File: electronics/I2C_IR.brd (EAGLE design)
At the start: 11 x 15.9 mm, 10 parts

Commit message: Revised board layout
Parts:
- removed U$1: ADC081C021, mes_adc:MSOP8_0.65
- added U1: ADC081C021, mes_adc:MSOP8_0.65
- moved C2 9.19 mm to (2.20, 3.30), turned to 180 degrees
- moved C4 1.80 mm to (8.70, 9.50), turned to 270 degrees
- moved C1 1.80 mm to (5.60, 3.30)
- moved C3 1.00 mm to (1.40, 9.50)
- moved JP3 1.00 mm to (5.50, 12.9)
- moved R1 1.00 mm to (2.90, 9.50)
- moved SJ1 1.00 mm to (1.50, 6.00)
- moved SJ2 1.00 mm to (9.50, 6.00)
- moved JP1 0.50 mm to (5.50, 1.10)
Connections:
- net ADR0: now also U1.3; no longer U$1.3
- net ADR1: now also U1.6; no longer U$1.6
- net ALERT: now also U1.2; no longer U$1.2
- net GND: now also U1.7; no longer U$1.7
- net N$4: now also U1.4; no longer U$1.4
- net SCL: now also U1.1; no longer U$1.1
- net SDA: now also U1.8; no longer U$1.8
- net VCC: now also U1.5; no longer U$1.5
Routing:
- net VCC: track 21.5 -> 36.2 mm
- net ADR1: track 5.62 -> 6.72 mm
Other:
- board size 11 x 15.9 mm -> 11 x 15.4 mm

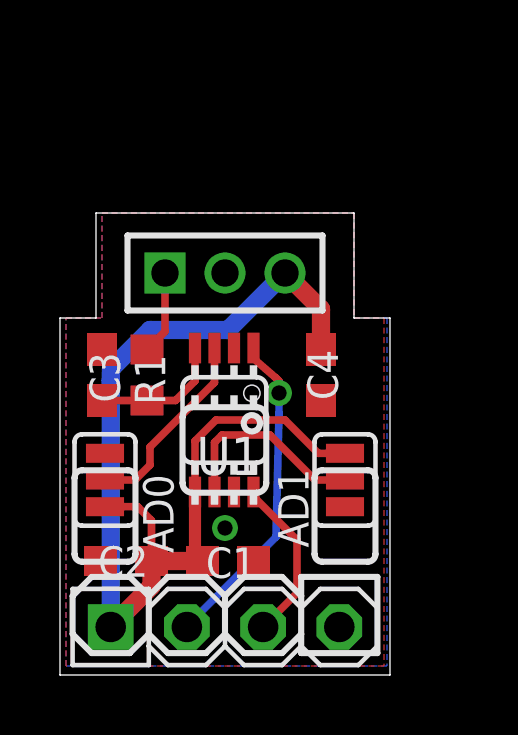
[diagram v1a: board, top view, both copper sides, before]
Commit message: Revised board layout per datasheet, single ground plane with join at chip ground location, no bottom traces, use tantalum bypass caps, etc.
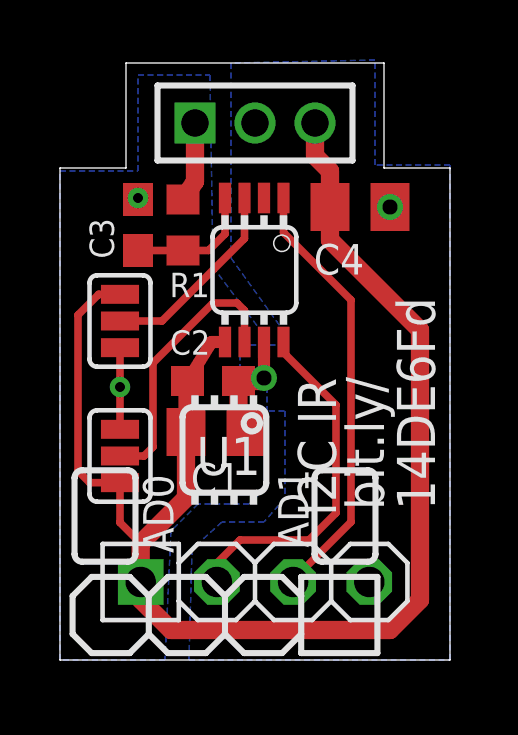
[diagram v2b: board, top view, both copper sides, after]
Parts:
- C1, C4: device rcl:C0603 -> rcl:C0805K
- SJ1: value ADR0 -> AD0
- SJ2: value ADR1 -> AD1
- moved SJ2 7.54 mm to (2.00, 6.80), turned to 90 degrees
- moved C2 6.66 mm to (5.10, 9.30), turned to 0 degrees
- moved C4 5.75 mm to (10.0, 15.1), turned to 0 degrees
- moved SJ1 5.32 mm to (2.00, 11.3), turned to 270 degrees
- moved C3 5.14 mm to (2.60, 14.5)
- moved R1 5.14 mm to (4.10, 14.5)
- moved U1 5.10 mm to (6.50, 13.0)
- moved JP3 5.10 mm to (6.50, 17.9)
- moved C1 4.32 mm to (5.20, 7.60)
- moved JP1 1.80 mm to (6.50, 2.60)
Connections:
- net SCL: now also JP1.3; no longer JP1.2
- net SDA: now also JP1.2; no longer JP1.3
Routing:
- net VCC: track 36.2 -> 48.6 mm
- net GND: track 0.00 -> 6.78 mm, vias 1 -> 4
- net SDA: track 5.57 -> 11.7 mm
- net SCL: track 10.9 -> 14.5 mm, vias 1 -> 0
- net ADR1: track 6.72 -> 9.13 mm
- removed copper zone on layer 1, net GND
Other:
- board size 11 x 15.4 mm -> 13 x 19.9 mm
- board text added: "14DE6Fd"
- board text added: "I2C IR"
- board text added: "bit.ly/"
